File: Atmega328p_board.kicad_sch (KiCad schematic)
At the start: 25 parts, among them U1 24LC1025, U2 24LC1025, U3 ATMEGA328P-AU, U4 DS1337S_, Y1 16MHz, Y2 32.768 KHz

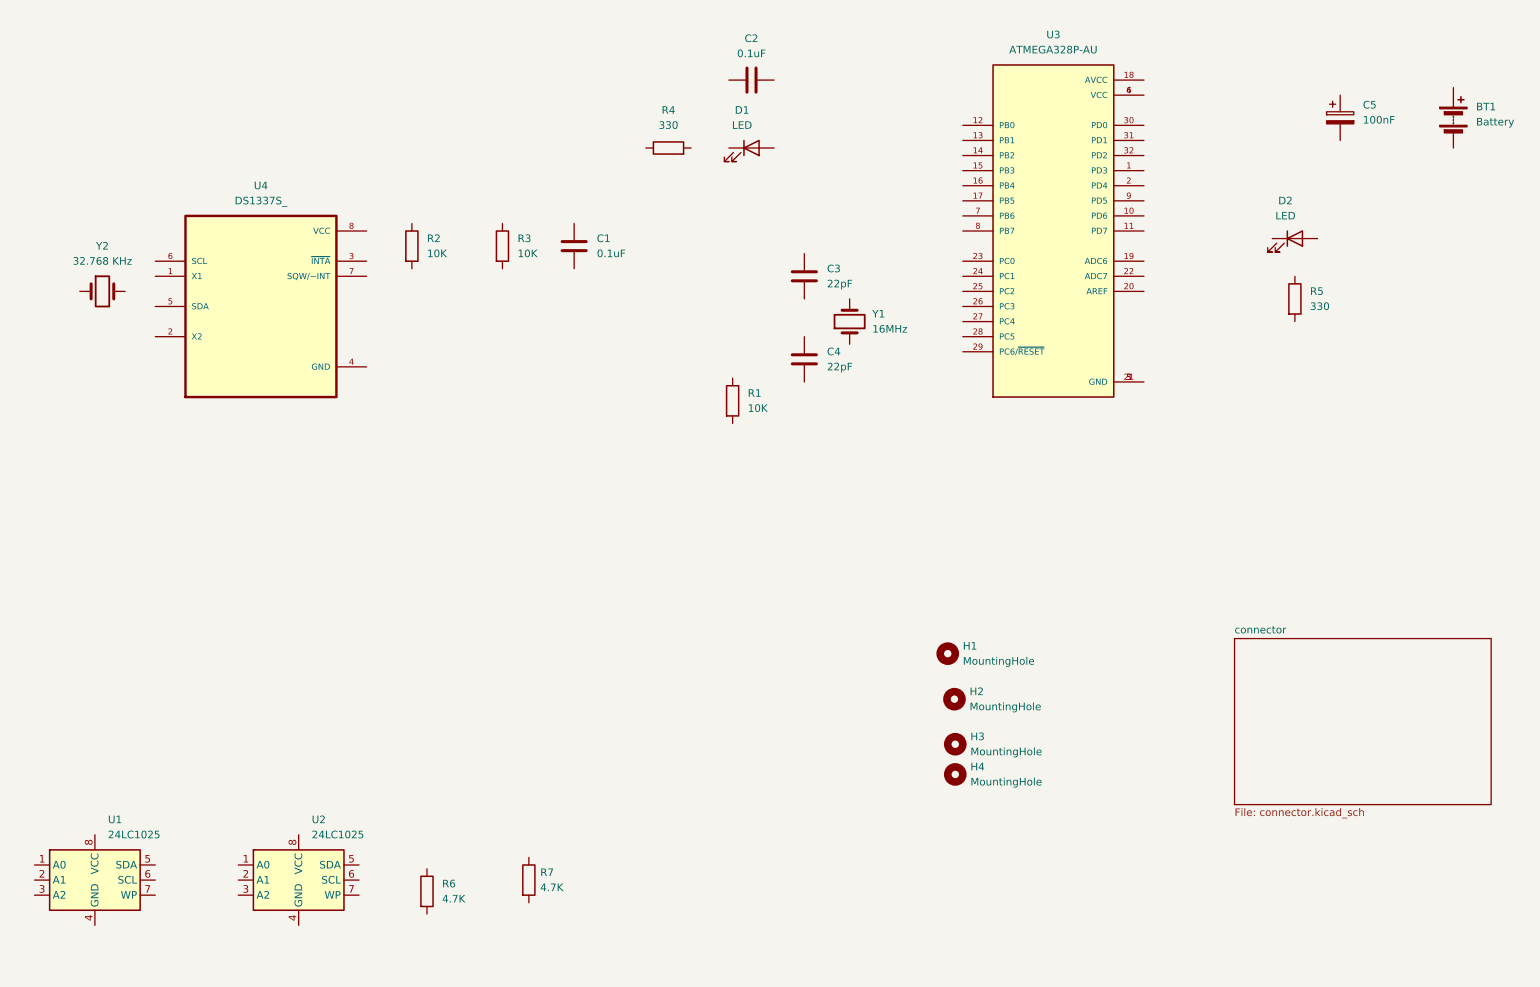
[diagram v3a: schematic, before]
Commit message: Completed wiring of sheet 1
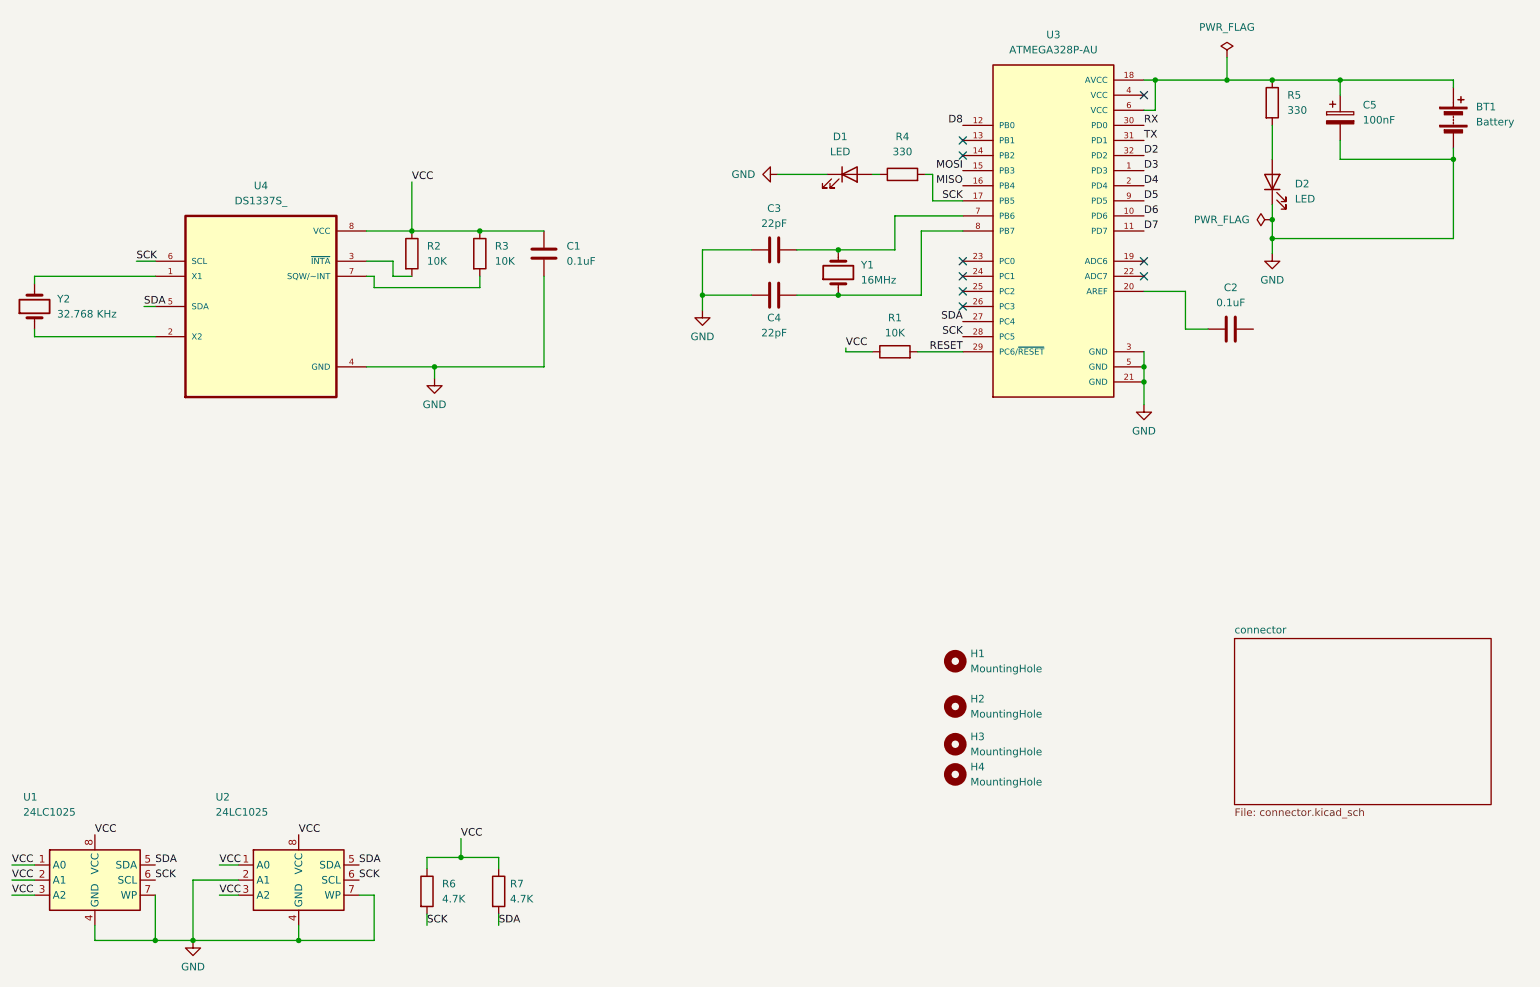
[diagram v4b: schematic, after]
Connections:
- net at C2.1: now also U3.20 (AREF)
- net VCC: now reaches U2.1 (A0)
- net VCC: now also C1.1, R1.1, R2.1, R3.1, R6.1, R7.1, U1.1 (A0), U1.2 (A1), U1.3 (A2), U1.8 (VCC), U2.3 (A2), U2.8 (VCC), U4.8 (VCC)
- net GND: now reaches U2.2 (A1)
- net GND: now also BT1.2 (-), C1.2, C3.1, C4.2, C5.2, D1.1 (K), D2.1 (K), U1.4 (GND), U1.7 (WP), U2.4 (GND), U2.7 (WP), U3.21 (GND), U3.3 (GND), U3.5 (GND), U4.4 (GND)
- net SDA: now reaches U2.5 (SDA)
- net SDA: now also R7.2, U1.5 (SDA), U3.27 (PC4), U4.5 (SDA)
- net SCK: now reaches U2.6 (SCL)
- net SCK: now also R4.2, R6.2, U1.6 (SCL), U3.17 (PB5), U3.28 (PC5), U4.6 (SCL)
- net at R4.1: now also D1.2 (A)
- net at R3.2: now also U4.7 (SQW/~INT)
- net at BT1.1 (+): now also C5.1, R5.1, U3.18 (AVCC), U3.6 (VCC)
- net at D2.2 (A): now also R5.2
- net at Y2.1: now also U4.2 (X2)
- net at Y2.2: now also U4.1 (X1)
- net at U4.3 (~{INTA}): now also R2.2
- net at C3.2: now also U3.7 (PB6), Y1.2
- net D3: now reaches U3.1 (PD3)
- net D6: now reaches U3.10 (PD6)
- net D7: now reaches U3.11 (PD7)
- net D8: now reaches U3.12 (PB0)
- net MOSI: now reaches U3.15 (PB3)
- net MISO: now reaches U3.16 (PB4)
- net D4: now reaches U3.2 (PD4)
- net RESET: now reaches U3.29 (PC6/~{RESET})
- net RESET: now also R1.2
- net RX: now reaches U3.30 (PD0)
- net TX: now reaches U3.31 (PD1)
- net D2: now reaches U3.32 (PD2)
- net at U3.4 (VCC): no longer U3.6 (VCC)
- net at U3.8 (PB7): now also C4.1, Y1.1
- net D5: now reaches U3.9 (PD5)
- no-connect marks 0 -> 9
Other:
- moved on the sheet: C1, C2, C3, C4, D1, D2, H1, H2, R1, R2, R3, R4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

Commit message: Completed wiring of sheet 2
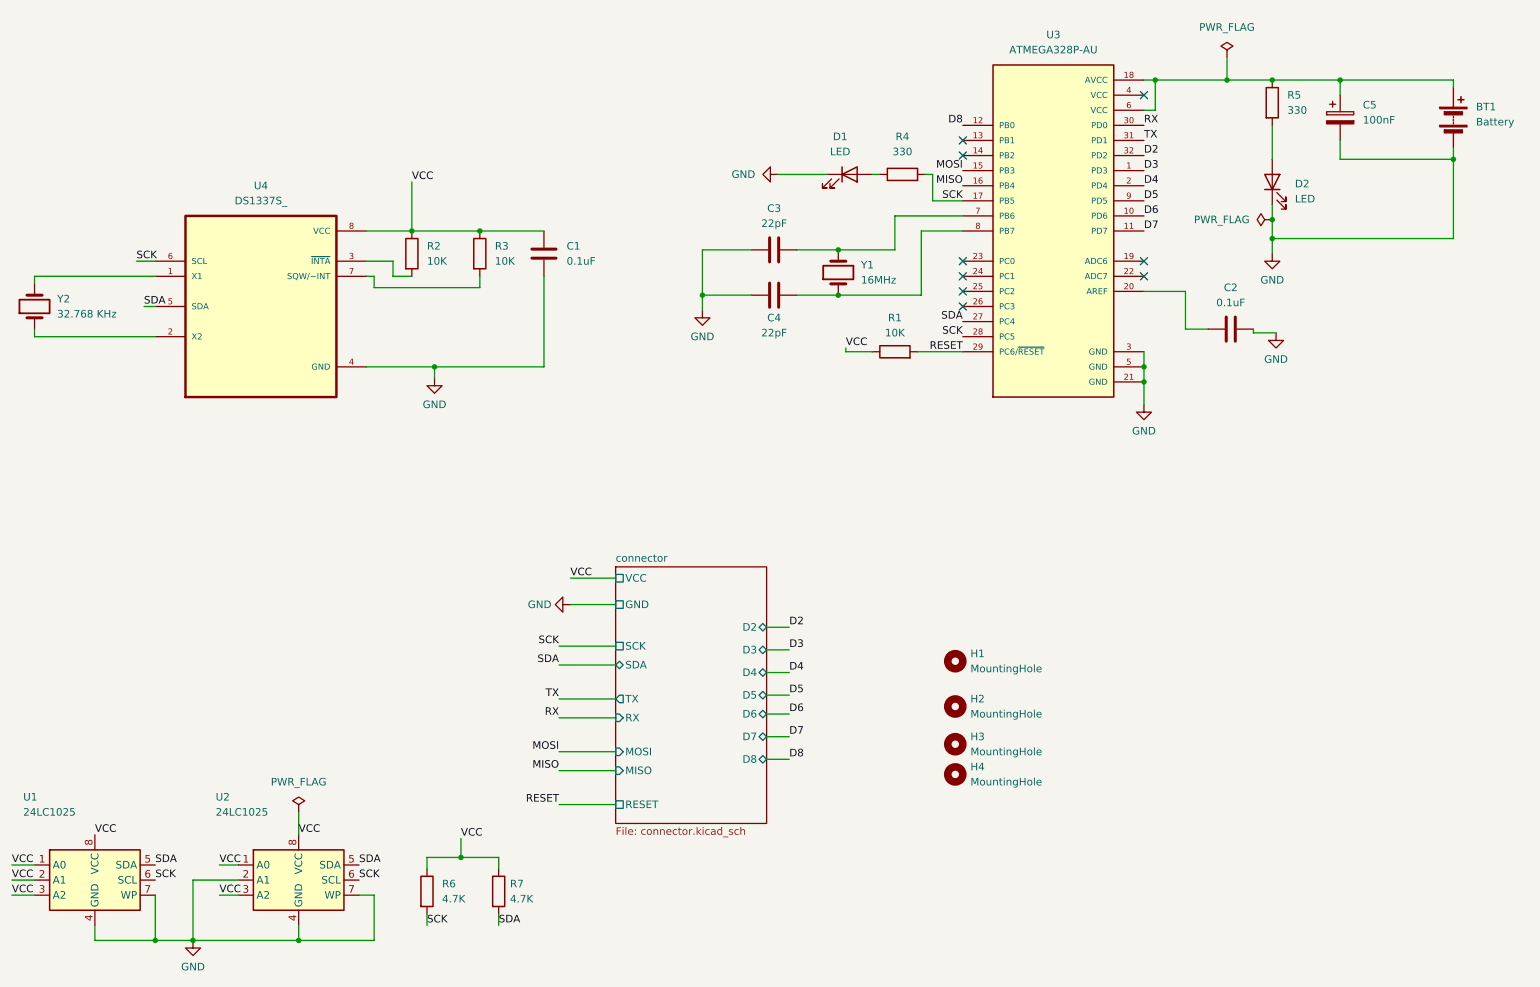
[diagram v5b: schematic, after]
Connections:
- net GND: now also C2.2
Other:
- sheet connector ports: added D2, D3, D4, D5, D6, D7, D8, GND, MISO, MOSI, RESET, RX, SCK, SDA, TX, VCC; removed none
